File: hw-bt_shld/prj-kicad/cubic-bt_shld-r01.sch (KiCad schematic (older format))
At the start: 2 parts

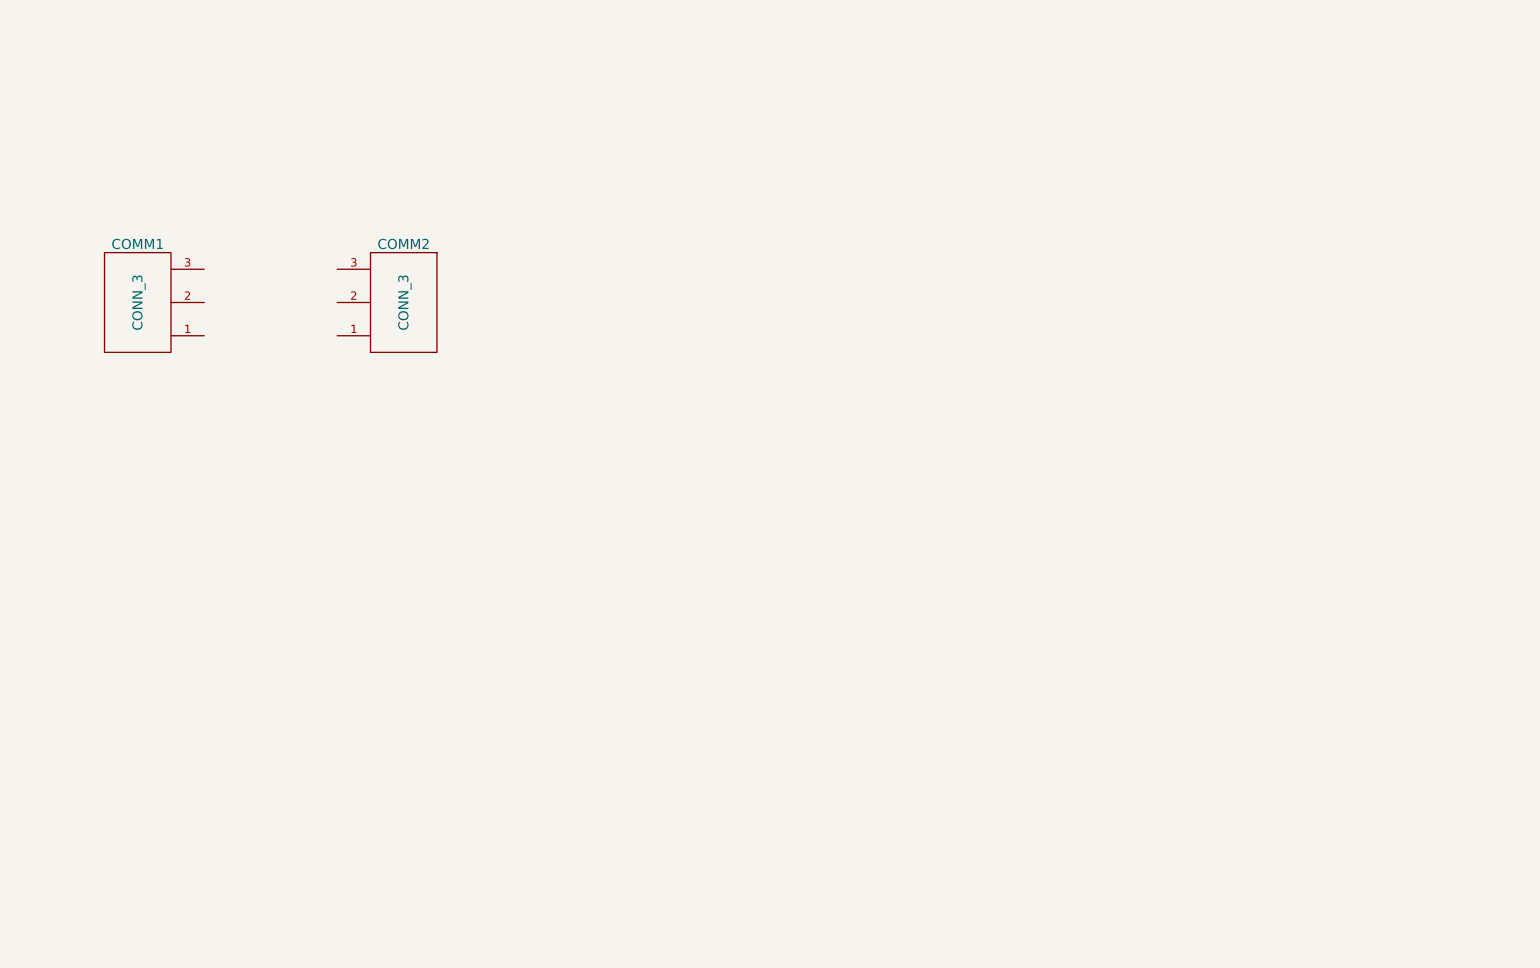
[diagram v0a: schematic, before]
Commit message: = UPD: Insert CC2540 and the HF interface to antenna
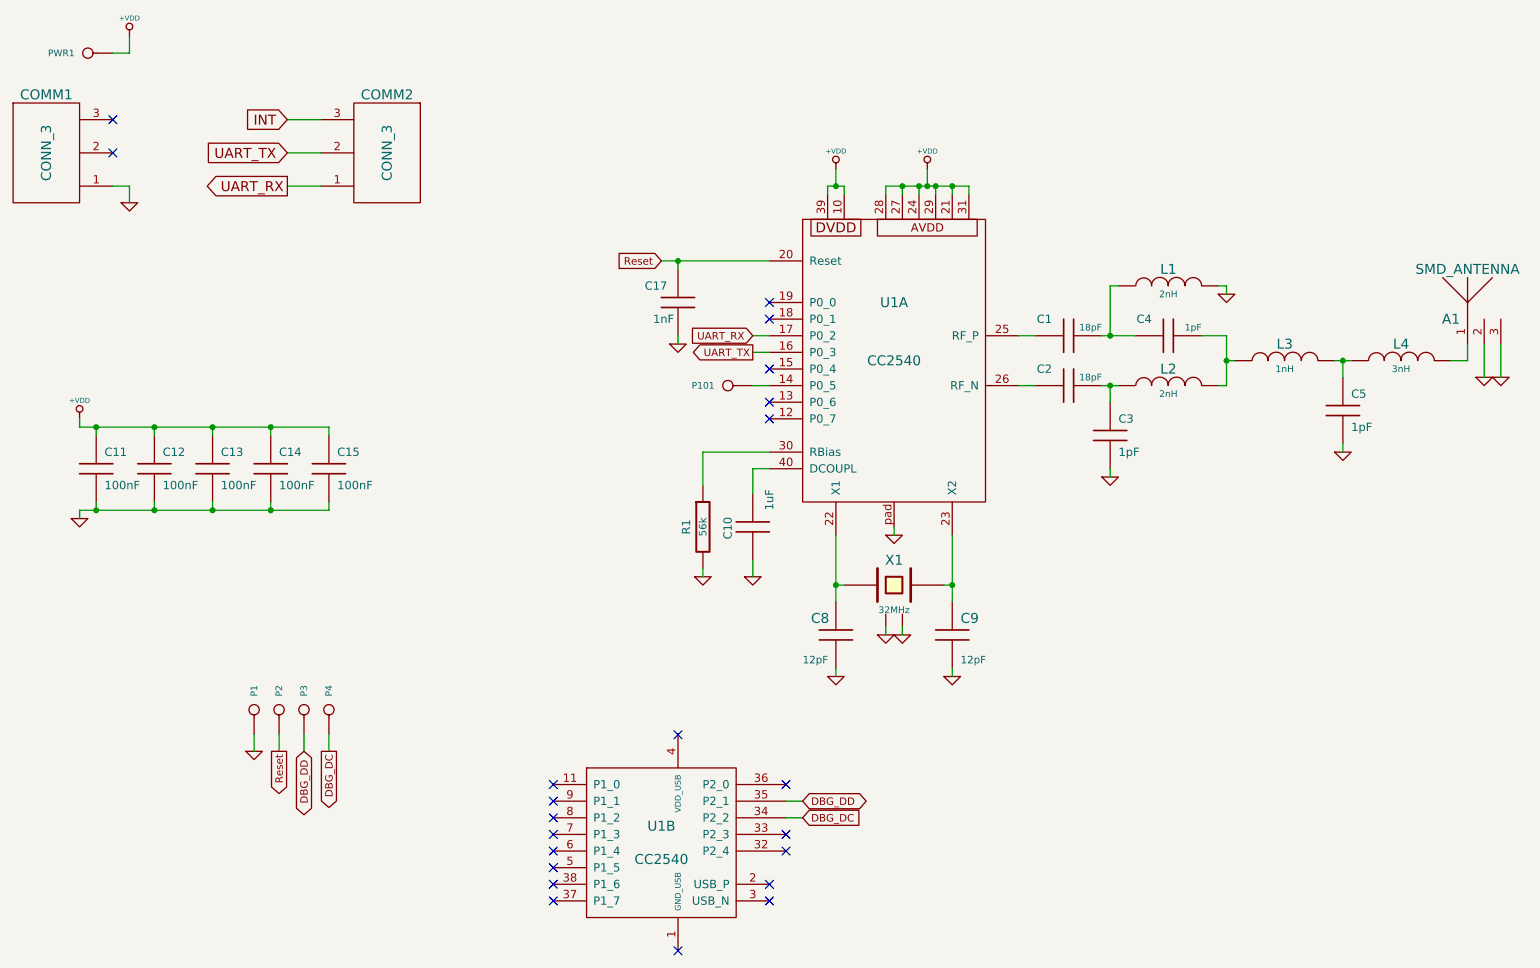
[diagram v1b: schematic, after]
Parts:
- added A1: SMD_ANTENNA, symbol SMD_ANTENNA
- added C1, C2: 18pF, symbol C
- added C10: 1uF, symbol C
- added C11, C12, C13, C14, C15: 100nF, symbol C
- added C17: 1nF, symbol C
- added C3, C4, C5: 1pF, symbol C
- added C8, C9: 12pF, symbol C
- added L1, L2: 2nH, symbol INDUCTOR
- added L3: 1nH, symbol INDUCTOR
- added L4: 3nH, symbol INDUCTOR
- added P1, P101, P2, P3, P4, PWR1: CONN_1, symbol CONN_1
- added R1: 56k, symbol R
- added U1: CC2540, symbol CC2540
- added X1: 32MHz, symbol CRYSTAL
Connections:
- net GND: now reaches COMM1.1
- net GND: now also A1.2, A1.3, C10.2, C11.2, C12.2, C13.2, C14.2, C15.2, C17.2, C3.2, C5.2, C8.2, C9.2, L1.2, P1.1, R1.2, U1.pad, X1.2, X1.4
- net UART_RX: now reaches COMM2.1
- net UART_RX: now also U1.17 (P0_2)
- net UART_TX: now reaches COMM2.2
- net UART_TX: now also U1.16 (P0_3)
- net INT: now reaches COMM2.3
- new net: P101.1, U1.14 (P0_5)
- new net: C8.1, U1.22 (X1), X1.1
- new net: C9.1, U1.23 (X2), X1.3
- new net: C1.1, U1.25 (RF_P)
- new net: C2.1, U1.26 (RF_N)
- new net: R1.1, U1.30 (RBias)
- new net: C10.1, U1.40 (DCOUPL)
- new net: C1.2, C4.1, L1.1
- new net: C2.2, C3.1, L2.1
- new net: C4.2, L2.2, L3.1
- new net: C5.1, L3.2, L4.1
- new net: A1.1, L4.2
- new net +VDD: C11.1, C12.1, C13.1, C14.1, C15.1, PWR1.1, U1.10, U1.21, U1.24, U1.27, U1.28, U1.29, U1.31, U1.39
- new net DBG_DC: P4.1, U1.34 (P2_2)
- new net DBG_DD: P3.1, U1.35 (P2_1)
- new net Reset: C17.1, P2.1, U1.20 (Reset)
- no-connect marks 0 -> 22
